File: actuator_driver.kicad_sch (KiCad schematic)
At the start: 9 parts, among them Q1 CSD19532Q5B, Q2 CSD19532Q5B, Q3 CSD19532Q5B, Q4 CSD19532Q5B, U1 FAN7389MX1

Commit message: new
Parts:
- added C1, C2: 10u, symbol Device:C
- added D1, D2: D, symbol Device:D
- added R5, R6: 5.1, symbol Device:R
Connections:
- net +12V: now also R5.1, R6.1
- net GND: now also U1.4 (HIN3), U1.7 (LIN3)
- net EN_Driver: now reaches U1.10 (EN)
- net HIN1: now reaches U1.2 (HIN1)
- net at U1.22 (VS2): now also C2.2
- net VB2: now reaches U1.24 (VB2)
- net VB2: now also C2.1, D2.1 (K)
- net at U1.26 (VS1): now also C1.2
- net VB1: now reaches U1.28 (VB1)
- net VB1: now also C1.1, D1.1 (K)
- net HIN2: now reaches U1.3 (HIN2)
- net LIN1: now reaches U1.5 (LIN1)
- net LIN2: now reaches U1.6 (LIN2)
- new net: D1.2 (A), R5.2
- new net: D2.2 (A), R6.2
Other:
- moved on the sheet: R1, R2

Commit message: new footprints
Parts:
- C1, C2: footprint (none) -> Capacitor_SMD:C_1210_3225Metric
- Q1, Q2, Q3, Q4: footprint Package_TO_SOT_SMD:TDSON-8-1 -> Heatsink:Heatsink_AAVID_573300D00010G_TO-263
- R1, R2: footprint (none) -> Heatsink:Heatsink_AAVID_573300D00010G_TO-263
- U1: footprint SOIC28_18X7P5_ONS -> (none)
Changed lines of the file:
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@@
 			)
 		)
-		(property "Footprint" ""
+		(property "Footprint" "Heatsink:Heatsink_AAVID_573300D00010G_TO-263"
 			(at 110.49 99.822 90)
 			(effects
@@
 			)
 		)
-		(property "Footprint" "SOIC28_18X7P5_ONS"
+		(property "Footprint" ""
 			(at 50.8 88.9 0)
 			(effects
@@
 			)
 		)
-		(property "Footprint" "Package_TO_SOT_SMD:TDSON-8-1"
+		(property "Footprint" "Heatsink:Heatsink_AAVID_573300D00010G_TO-263"
 			(at 191.77 99.695 0)
 			(effects
@@
 			)
 		)
-		(property "Footprint" "Package_TO_SOT_SMD:TDSON-8-1"
+		(property "Footprint" "Heatsink:Heatsink_AAVID_573300D00010G_TO-263"
 			(at 160.02 103.505 0)
 			(effects
@@
 			)
 		)
-		(property "Footprint" "Package_TO_SOT_SMD:TDSON-8-1"
+		(property "Footprint" "Heatsink:Heatsink_AAVID_573300D00010G_TO-263"
 			(at 160.02 81.915 0)
 			(effects
@@
 			)
 		)
-		(property "Footprint" ""
+		(property "Footprint" "Capacitor_SMD:C_1210_3225Metric"
 			(at 101.2952 105.41 0)
 			(effects
@@
 			)
 		)
-		(property "Footprint" "Package_TO_SOT_SMD:TDSON-8-1"
+		(property "Footprint" "Heatsink:Heatsink_AAVID_573300D00010G_TO-263"
 			(at 191.77 78.105 0)
 			(effects
@@
 			)
 		)
-		(property "Footprint" ""
+		(property "Footprint" "Heatsink:Heatsink_AAVID_573300D00010G_TO-263"
 			(at 110.49 89.662 90)
 			(effects
@@
 			)
 		)
-		(property "Footprint" ""
+		(property "Footprint" "Capacitor_SMD:C_1210_3225Metric"
 			(at 101.2952 87.63 0)
 			(effects

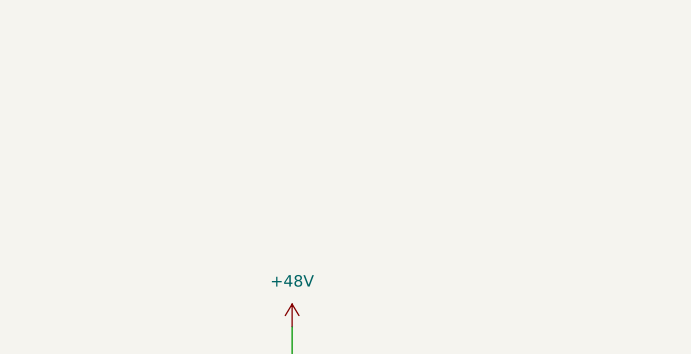
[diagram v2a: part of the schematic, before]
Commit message: new XT60 connector
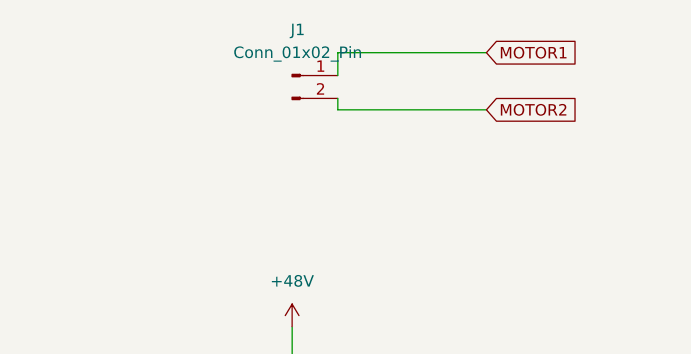
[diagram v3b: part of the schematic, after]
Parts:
- added J1: Conn_01x02_Pin, Connector_AMASS:AMASS_XT60IPW-M_1x03_P7.20mm_Horizontal, symbol Connector:Conn_01x02_Pin
- D1: footprint (none) -> Connector_AMASS:AMASS_XT60IPW-M_1x03_P7.20mm_Horizontal
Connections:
- net MOTOR1: now also J1.1 (Pin_1)
- net MOTOR2: now also J1.2 (Pin_2)
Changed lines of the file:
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@@
+	(wire
+		(pts
+			(xy 195.58 41.91) (xy 179.07 41.91)
+		)
+		(stroke
+			(width 0)
+			(type default)
+		)
+	)
 	(wire
 		(pts
@@
 	(wire
 		(pts
+			(xy 195.58 35.56) (xy 179.07 35.56)
+		)
+		(stroke
+			(width 0)
+			(type default)
+		)
+	)
+	(wire
+		(pts
 			(xy 50.8 96.52) (xy 44.45 96.52)
 		)
@@
 	(wire
 		(pts
+			(xy 179.07 35.56) (xy 179.07 38.1)
+		)
+		(stroke
+			(width 0)
+			(type default)
+		)
+	)
+	(wire
+		(pts
 			(xy 92.71 43.18) (xy 97.79 43.18)
 		)
@@
 		(pts
 			(xy 91.44 97.79) (xy 91.44 99.06)
+		)
+		(stroke
+			(width 0)
+			(type default)
+		)
+	)
+	(wire
+		(pts
+			(xy 179.07 41.91) (xy 179.07 40.64)
 		)
 		(stroke
@@
 		)
 	)
+	(global_label "MOTOR2"
+		(shape input)
+		(at 195.58 41.91 0)
+		(fields_autoplaced yes)
+		(effects
+			(font
+				(size 1.27 1.27)
+			)
+			(justify left)
+		)
+		(property "Intersheetrefs" "${INTERSHEET_REFS}"
+			(at 206.1247 41.91 0)
+			(effects
+				(font
+					(size 1.27 1.27)
+				)
+				(justify left)
+				(hide yes)
+			)
+		)
+	)
 	(global_label "HO1"
 		(shape input)
@@
 				)
 				(justify right)
+				(hide yes)
+			)
+		)
+	)
+	(global_label "MOTOR1"
+		(shape input)
+		(at 195.58 35.56 0)
+		(fields_autoplaced yes)
+		(effects
+			(font
+				(size 1.27 1.27)
+			)
+			(justify left)
+		)
+		(property "Intersheetrefs" "${INTERSHEET_REFS}"
+			(at 206.1247 35.56 0)
+			(effects
+				(font
+					(size 1.27 1.27)
+				)
+				(justify left)
 				(hide yes)
 			)
@@
 			)
 		)
-		(property "Footprint" ""
+		(property "Footprint" "Connector_AMASS:AMASS_XT60IPW-M_1x03_P7.20mm_Horizontal"
 			(at 92.71 54.61 0)
 			(effects
@@
 					(unit 1)
 				)
+			)
+		)
+	)
+	(symbol
+		(lib_id "Connector:Conn_01x02_Pin")
+		(at 173.99 38.1 0)
+		(unit 1)
+		(exclude_from_sim no)
+		(in_bom yes)
+		(on_board yes)
+		(dnp no)
+		(fields_autoplaced yes)
+		(property "Reference" "J1"
+			(at 174.625 33.02 0)
+			(effects
+				(font
+					(size 1.27 1.27)
+				)
+			)
+		)
+		(property "Value" "Conn_01x02_Pin"
+			(at 174.625 35.56 0)
+			(effects
+				(font
+					(size 1.27 1.27)
+				)
+			)
+		)
+		(property "Footprint" "Connector_AMASS:AMASS_XT60IPW-M_1x03_P7.20mm_Horizontal"
+			(at 173.99 38.1 0)
+			(effects
+				(font
+					(size 1.27 1.27)
+				)
+				(hide yes)
+			)
+		)
+		(property "Datasheet" "~"
+			(at 173.99 38.1 0)
+			(effects
+				(font
+					(size 1.27 1.27)
+				)
+				(hide yes)
+			)
+		)
+		(property "Description" "Generic connector, single row, 01x02, script generated"
+			(at 173.99 38.1 0)
+			(effects
+				(font
+					(size 1.27 1.27)
+				)
+				(hide yes)
+			)
+		)
+		(pin "1"
+		)
+		(pin "2"
+		)
+		(instances
+			(project ""
+				(path "/1ba1454e-567a-4f9c-a992-2d7ff779e1ef"
+					(reference "J1")
+					(unit 1)
+				)

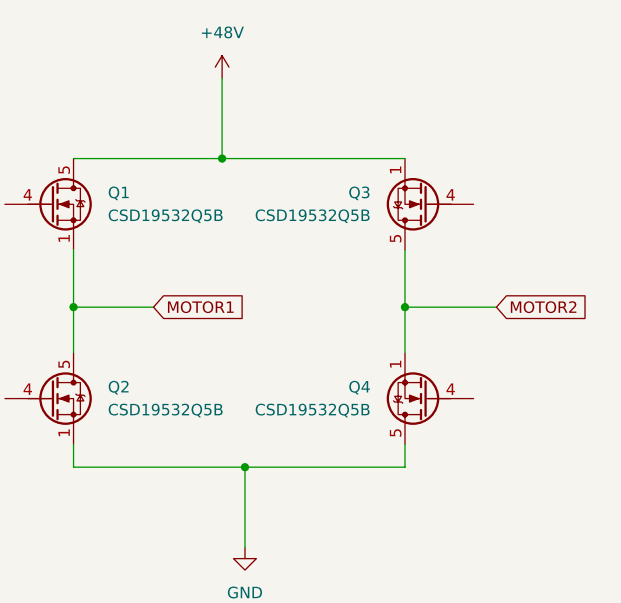
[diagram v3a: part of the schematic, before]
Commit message: new XT60 connector
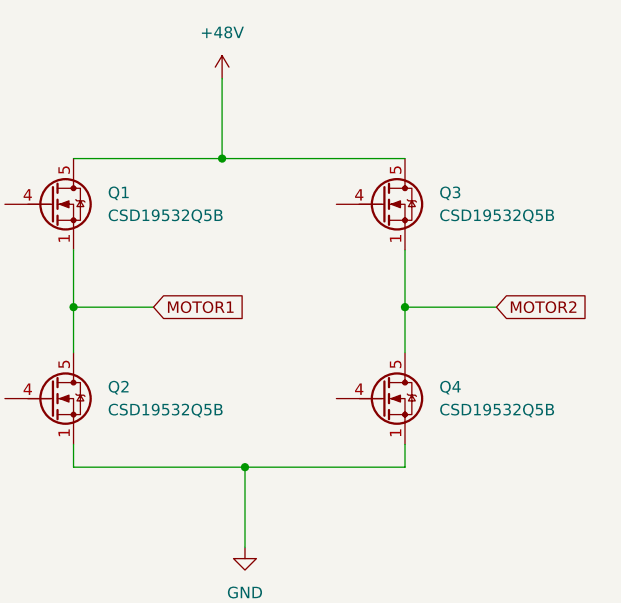
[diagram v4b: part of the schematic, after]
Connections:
- net +48V: now also Q3.5 (D); no longer Q3.1 (S), Q3.2 (S), Q3.3 (S)
- net GND: now also Q4.1 (S), Q4.2 (S), Q4.3 (S); no longer Q4.5 (D)
- net MOTOR2: now also Q3.1 (S), Q3.2 (S), Q3.3 (S), Q4.5 (D); no longer Q3.5 (D), Q4.1 (S), Q4.2 (S), Q4.3 (S)
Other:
- moved on the sheet: Q3, Q4
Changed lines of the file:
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@@
 	(symbol
 		(lib_id "Transistor_FET:CSD19532Q5B")
-		(at 196.85 101.6 180)
+		(at 191.77 101.6 0)
 		(unit 1)
 		(exclude_from_sim no)
@@
 		(fields_autoplaced yes)
 		(property "Reference" "Q4"
-			(at 190.5 100.3299 0)
+			(at 198.12 100.3299 0)
 			(effects
 				(font
@@
 		)
 		(property "Value" "CSD19532Q5B"
-			(at 190.5 102.8699 0)
+			(at 198.12 102.8699 0)
 			(effects
 				(font
@@
 		)
 		(property "Footprint" "Heatsink:Heatsink_AAVID_573300D00010G_TO-263"
-			(at 191.77 99.695 0)
+			(at 196.85 103.505 0)
 			(effects
 				(font
@@
 		)
 		(property "Datasheet" "http://www.ti.com/lit/gpn/csd19532q5b"
-			(at 191.77 97.79 0)
+			(at 196.85 105.41 0)
 			(effects
 				(font
@@
 		)
 		(property "Description" "100A Id, 100V Vds, NexFET N-Channel Power MOSFET, 4.9mOhm Ron, 48nC Qg(typ), SON8 5x6mm"
-			(at 196.85 101.6 0)
+			(at 191.77 101.6 0)
 			(effects
 				(font
@@
 	(symbol
 		(lib_id "Transistor_FET:CSD19532Q5B")
-		(at 196.85 80.01 180)
+		(at 191.77 80.01 0)
 		(unit 1)
 		(exclude_from_sim no)
@@
 		(fields_autoplaced yes)
 		(property "Reference" "Q3"
-			(at 190.5 78.7399 0)
+			(at 198.12 78.7399 0)
 			(effects
 				(font
@@
 		)
 		(property "Value" "CSD19532Q5B"
-			(at 190.5 81.2799 0)
+			(at 198.12 81.2799 0)
 			(effects
 				(font
@@
 		)
 		(property "Footprint" "Heatsink:Heatsink_AAVID_573300D00010G_TO-263"
-			(at 191.77 78.105 0)
+			(at 196.85 81.915 0)
 			(effects
 				(font
@@
 		)
 		(property "Datasheet" "http://www.ti.com/lit/gpn/csd19532q5b"
-			(at 191.77 76.2 0)
+			(at 196.85 83.82 0)
 			(effects
 				(font
@@
 		)
 		(property "Description" "100A Id, 100V Vds, NexFET N-Channel Power MOSFET, 4.9mOhm Ron, 48nC Qg(typ), SON8 5x6mm"
-			(at 196.85 80.01 0)
-			(effects
-				(font
+			(at 191.77 80.01 0)
+			(effects
+				(font

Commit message: latest schematic
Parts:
- added C3: 5n, Capacitor_SMD:C_1206_3216Metric_Pad1.33x1.80mm_HandSolder, symbol Device:C
- added R11, R7, R8, R9: 1k, Resistor_SMD:R_1206_3216Metric_Pad1.30x1.75mm_HandSolder, symbol Device:R
- C1, C2: value 10u -> 1u
- D1: value D -> SS110; footprint Connector_AMASS:AMASS_XT60IPW-M_1x03_P7.20mm_Horizontal -> Diode_SMD:D_SMA
- D2: value D -> SS110; footprint (none) -> Diode_SMD:D_SMA
- Q1, Q2, Q3, Q4: footprint Heatsink:Heatsink_AAVID_573300D00010G_TO-263 -> Package_TO_SOT_SMD:TO-263-2
- R1, R2: value R -> 10; footprint Heatsink:Heatsink_AAVID_573300D00010G_TO-263 -> Resistor_SMD:R_1206_3216Metric_Pad1.30x1.75mm_HandSolder
- R3, R4: value R -> 10; footprint (none) -> Resistor_SMD:R_1206_3216Metric_Pad1.30x1.75mm_HandSolder
- R5, R6: footprint (none) -> Resistor_SMD:R_1206_3216Metric_Pad1.30x1.75mm_HandSolder
- U1: footprint (none) -> Package_SO:SOIC-28W_7.5x17.9mm_P1.27mm
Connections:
- net GND: now also U1.9 (*CS), C3.2, R8.2, R9.2
- net HO1: now also Q1.4 (G), R11.1
- net HO2: now also Q3.4 (G), R7.1
- net LO1: now also Q2.4 (G), R8.1
- net LO2: now also Q4.4 (G), R9.1
- net MOTOR1: now also R11.2
- net MOTOR2: now also R7.2
- net at U1.11 (RCIN): now also C3.1
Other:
- moved on the sheet: C1, C2, D1, D2, J1, Q1, Q2, Q3, Q4, R1, R2, R3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

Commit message: jitthi takeover
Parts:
- removed Q1, Q2, Q3, Q4: CSD19532Q5B, Package_TO_SOT_SMD:TO-263-2, symbol Transistor_FET:CSD19532Q5B
- added Q1, Q5, Q6, Q7: IRF540N, Package_TO_SOT_SMD:TO-263-2, symbol Transistor_FET:IRF540N
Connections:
- net +48V: now also Q1.2 (D), Q5.2 (D)
- net GND: now also Q6.3 (S), Q7.3 (S)
- net HO1: now also Q1.1 (G)
- net HO2: now also Q5.1 (G)
- net LO1: now also Q6.1 (G)
- net LO2: now also Q7.1 (G)
- net MOTOR1: now also Q6.2 (D)
- net MOTOR2: now also Q5.3 (S), Q7.2 (D)
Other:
- moved on the sheet: R11
